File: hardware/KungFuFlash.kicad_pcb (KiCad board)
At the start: 2 copper layers, 62 x 83.6 mm, 46 parts, among them J1 USB Power, J2 USB_B_Mini, J4 SWD, Q1 BC817, SW1 Reset, SW2 Menu, SW3 Special, U1 C64-Exp-Port, U2 AMS1117-3.3, U3 STM32F405RGTx, Y1 8MHz

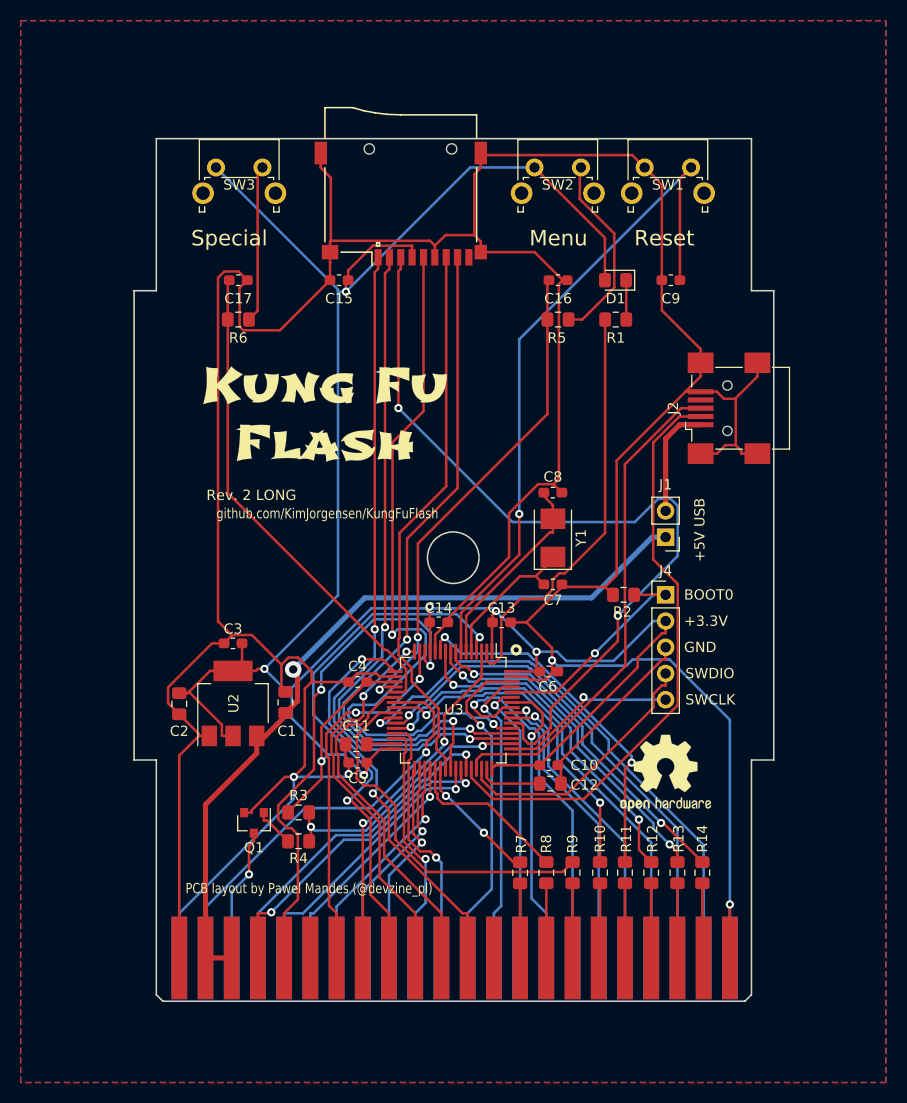
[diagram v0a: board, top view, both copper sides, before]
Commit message: GND layers adjustments.
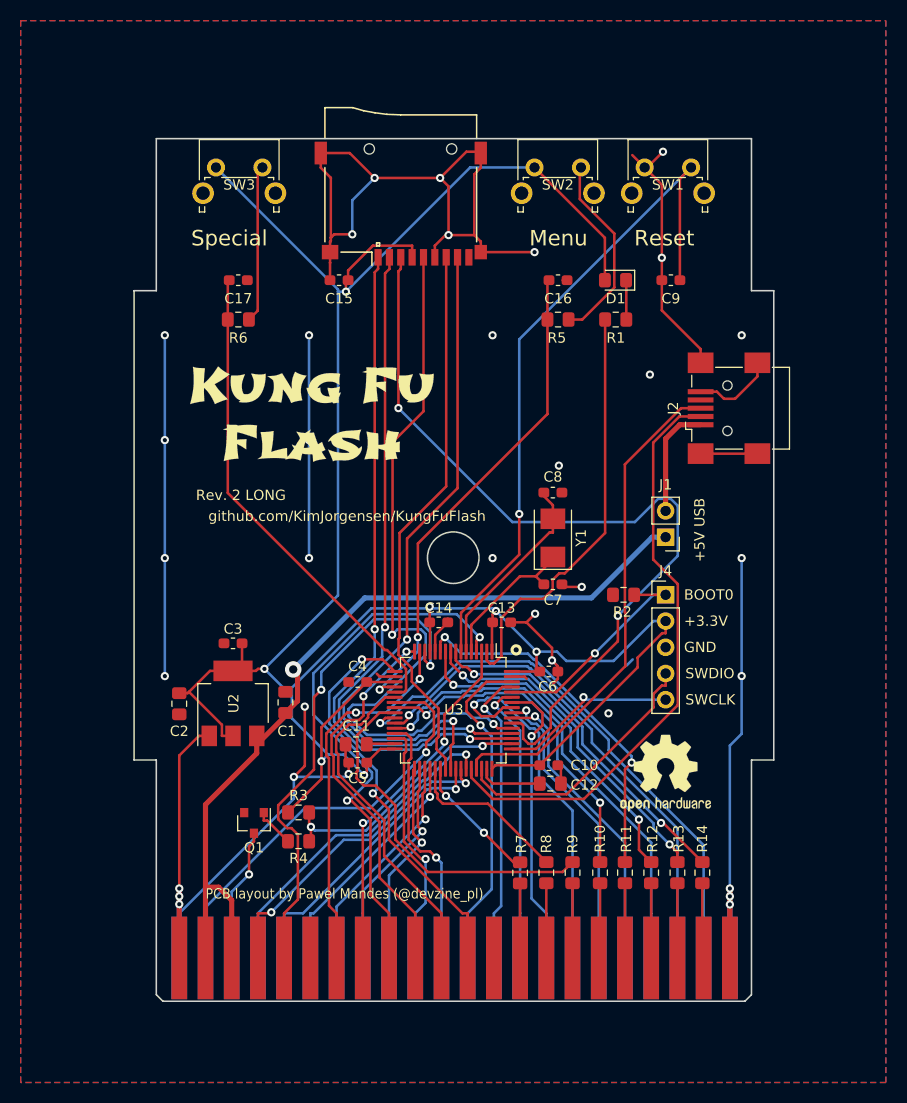
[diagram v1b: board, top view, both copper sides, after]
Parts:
- moved G*** 1.27 mm to (86.7, 82.9)
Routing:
- net GND: track 425.5 -> 295.4 mm, vias 4 -> 34
- net +5V: track 76.6 -> 82.7 mm
